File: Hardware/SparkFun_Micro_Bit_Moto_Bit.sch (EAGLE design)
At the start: 37 parts, among them J1 5.5x2.1mm Barrel, J2 CORTEX_DEBUGPTH, U1 CY8C4245LQI-483, U2 TPS62172, U3 micro:bit, U4 DRV8835

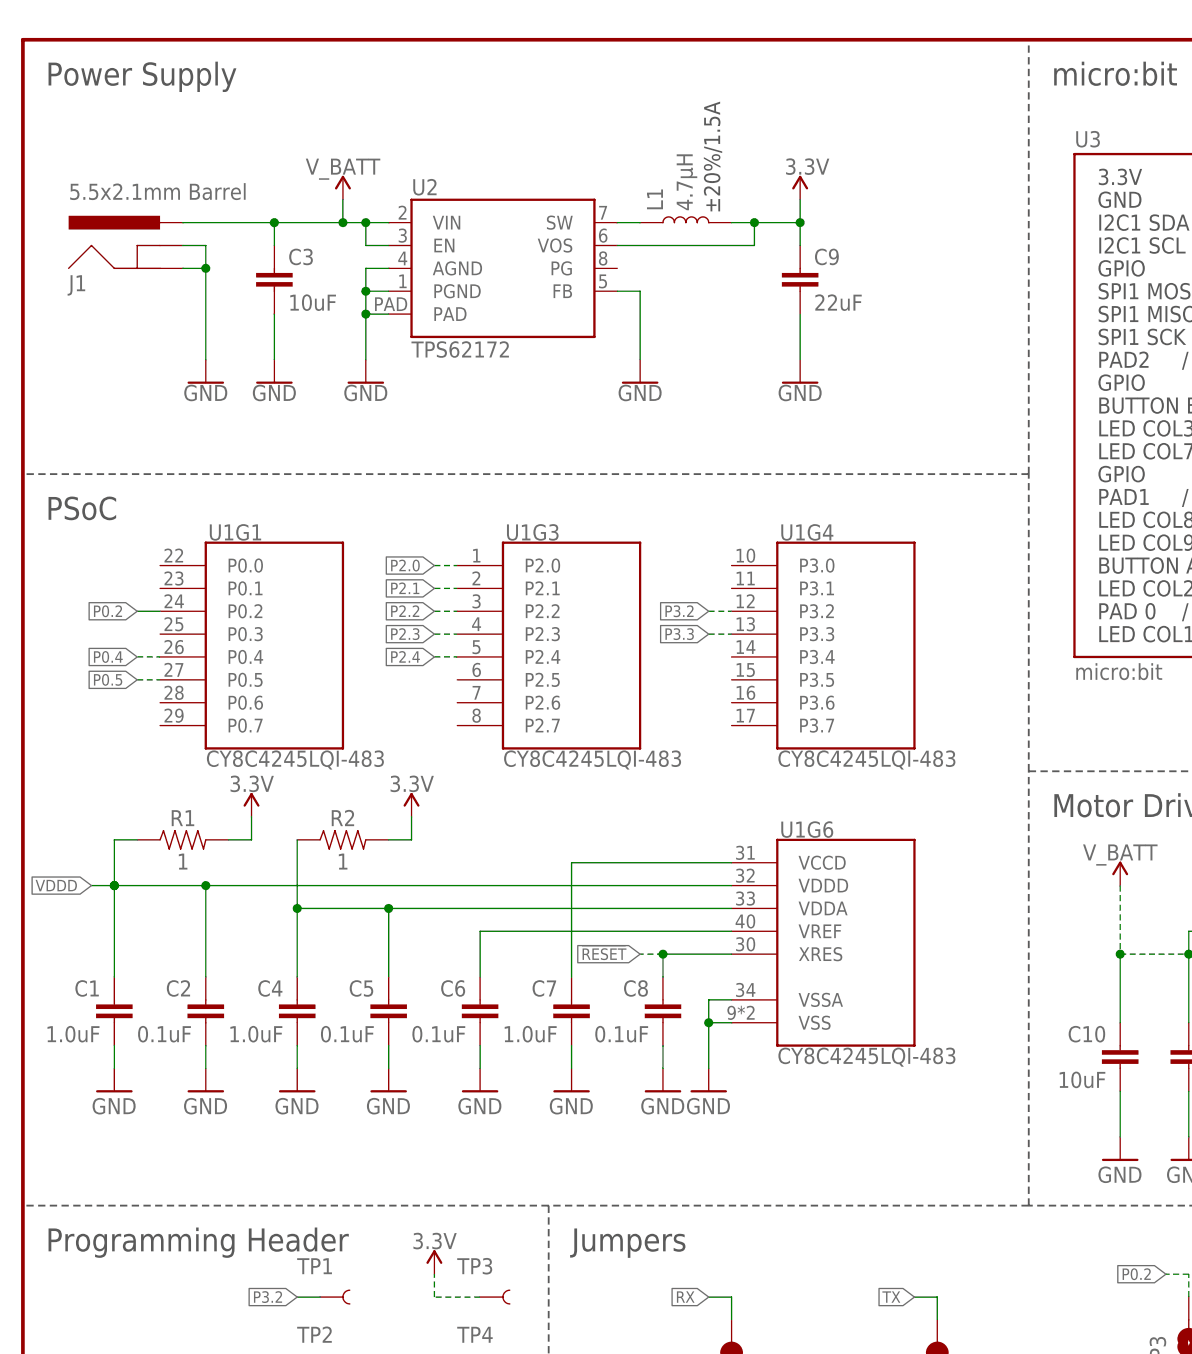
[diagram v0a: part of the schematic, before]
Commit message: Changed name from motobit to follow naming conventions
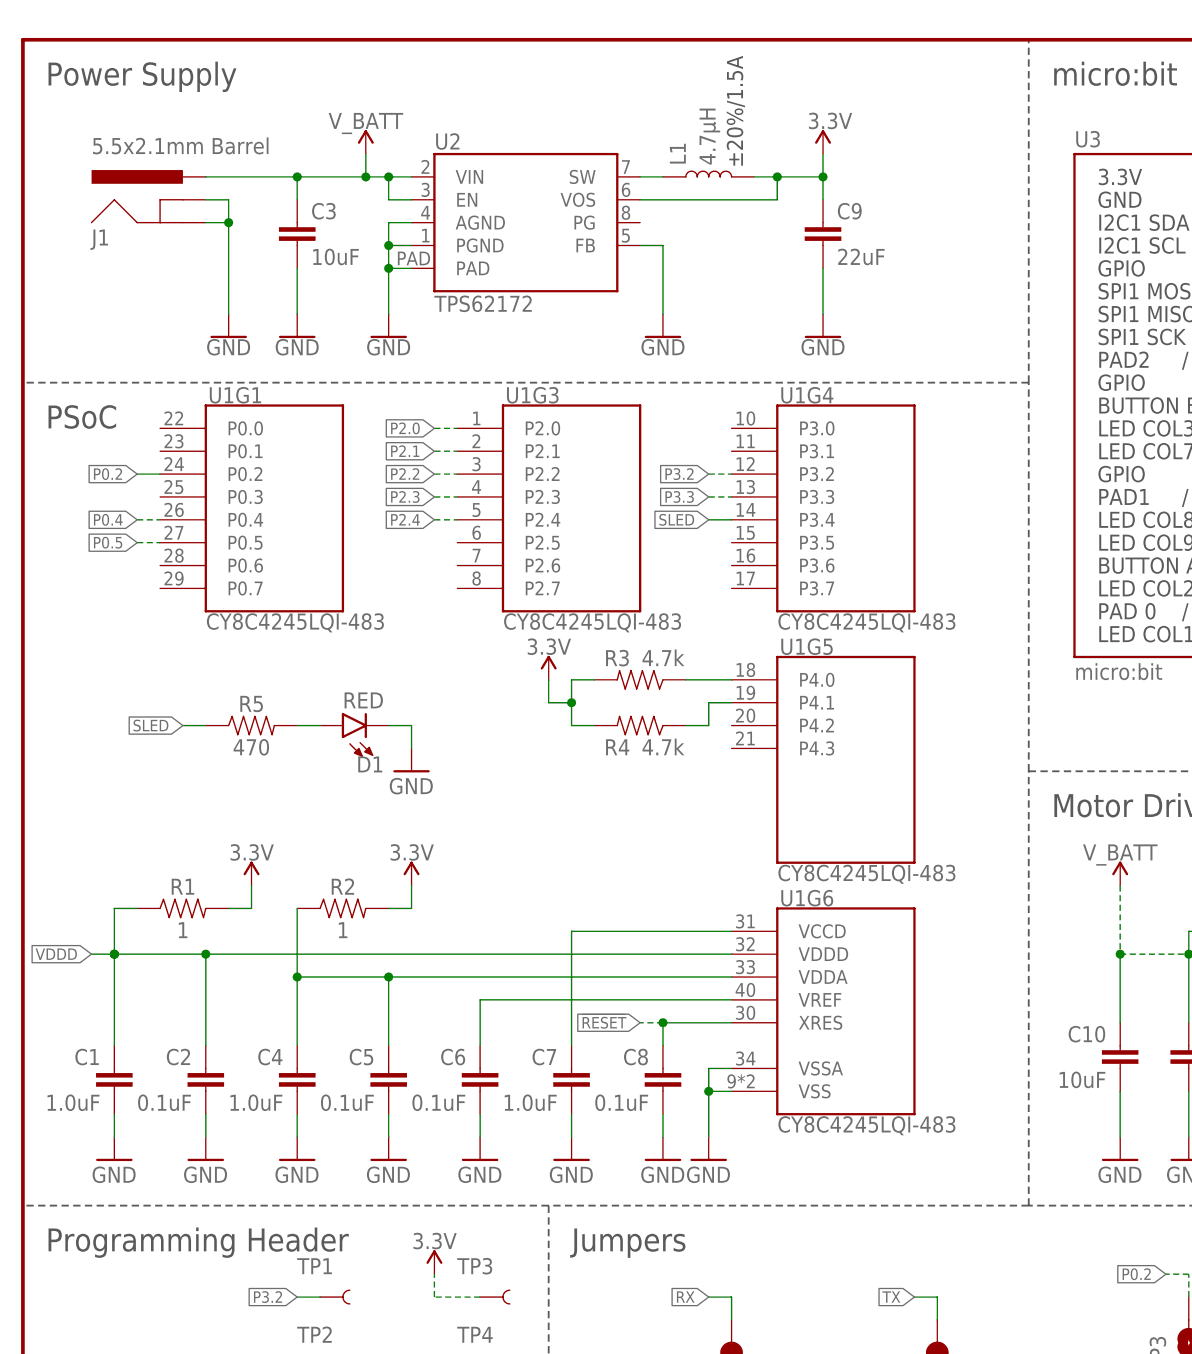
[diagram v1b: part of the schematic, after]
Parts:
- added D1: RED, SparkFun-LED:LED-RED0603
- added R3, R4: 4.7k, SparkFun-Resistors:4.7KOHM-0603-1/10W-1%
- added R5: 470, SparkFun-Resistors:470OHM-0603-1/10W-1%
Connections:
- new net N$6: R3.1, U1G5.P4.0
- new net N$7: R4.1, U1G5.P4.1
- new net N$8: D1.A, R5.2
- new net SLED: R5.1, U1G4.P3.4
- net 3.3V: now also R3.2, R4.2
- net GND: now also D1.C
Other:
- moved on the sheet: C1, C2, C3, C4, C5, C6, C7, C8, C9, J1, L1, R1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

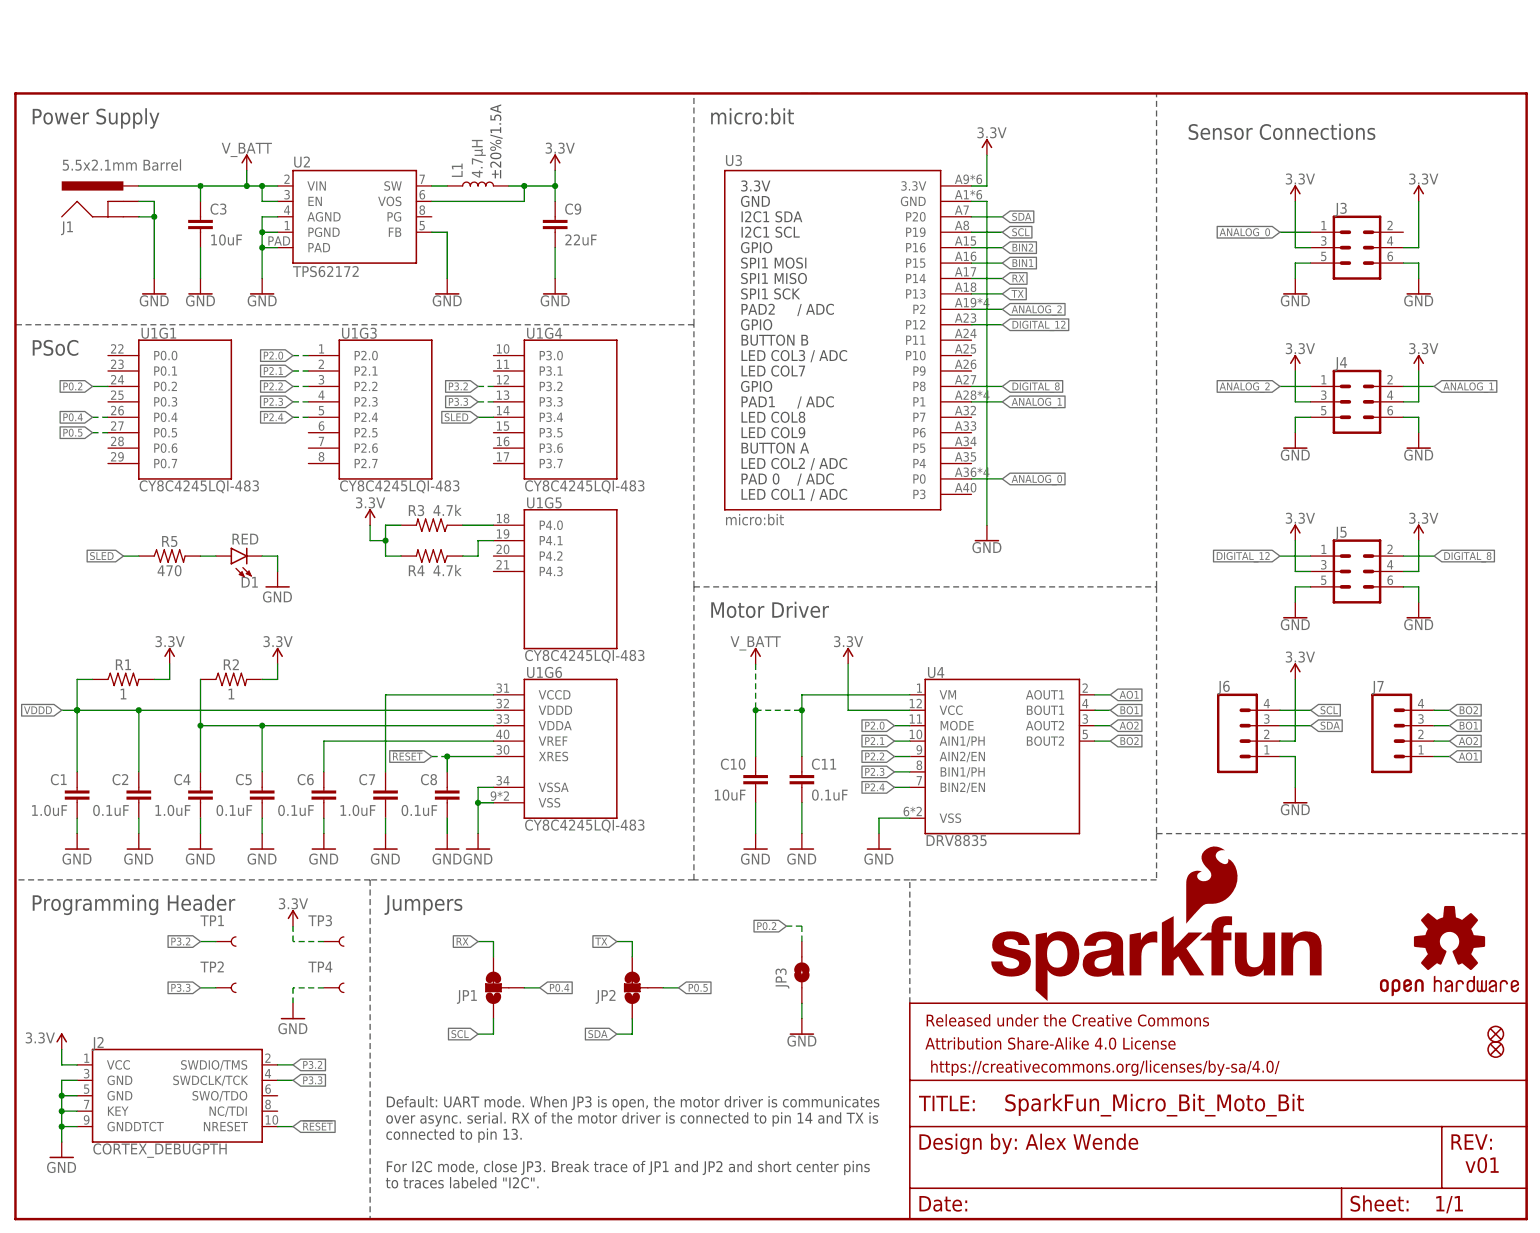
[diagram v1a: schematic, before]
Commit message: Design Review Changes
- Added staking vias to barrel connector and motor connector
- Added two servo connectors
- Moved vias that were exposed for motor driver heatsink
- Added selective solder path
- Added mounting holes
- Rounded corners to match micro:bit
- Rotated silk to match micro:bit silk orientation
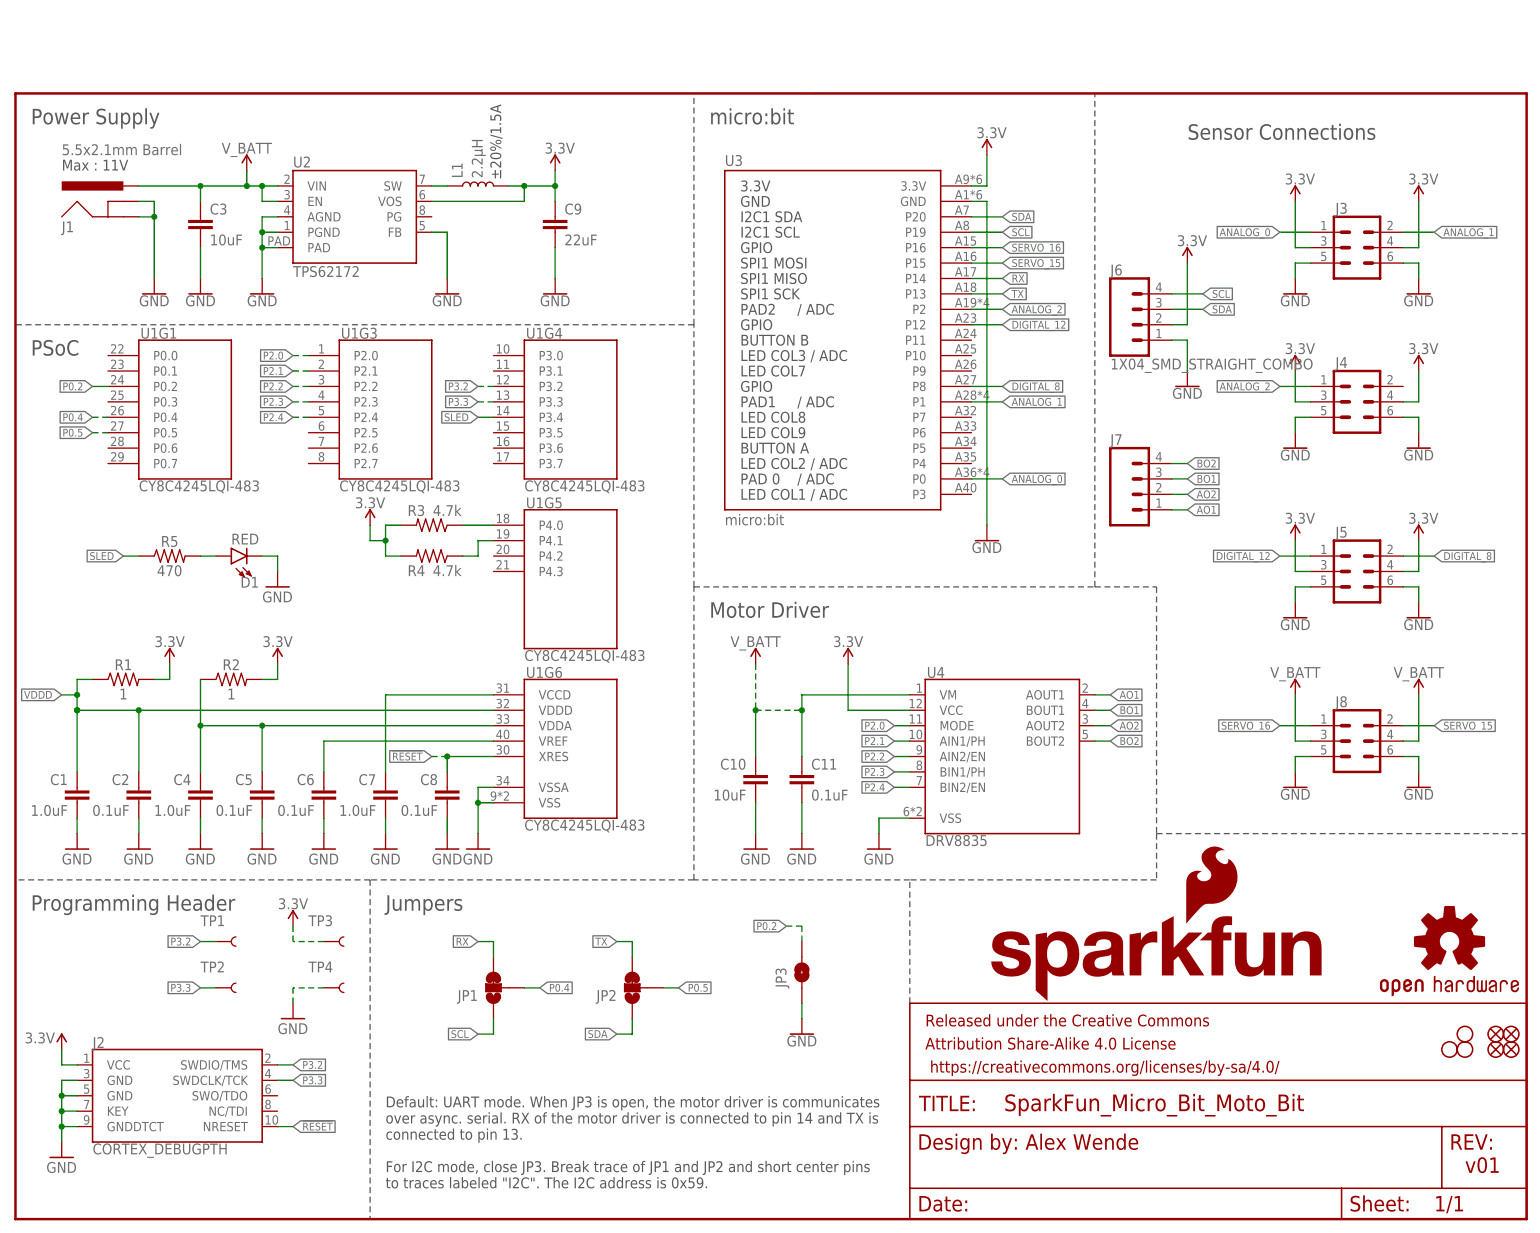
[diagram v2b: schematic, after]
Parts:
- added FD3, FD4: FIDUCIALUFIDUCIAL, SparkFun-Aesthetics:FIDUCIALUFIDUCIAL
- added H2, H3, H4: STAND-OFF, SparkFun-Hardware:STAND-OFF
- added J8: (no value), SparkFun-Connectors:CONN_03X2FEMALE_SMD
- J6: value (none) -> 1X04_SMD_STRAIGHT_COMBO
- L1: value 4.7µH -> 2.2µH
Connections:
- removed net BIN1: U3.P15
- removed net BIN2: U3.P16
- new net SERVO_15: J8.2, U3.P15
- new net SERVO_16: J8.1, U3.P16
- net ANALOG_1: now also J3.2; no longer J4.2
- net GND: now also J8.5, J8.6
- net V_BATT: now also J8.3, J8.4
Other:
- note added: "Default: UART mode. When JP3 is open, the motor driver is communicates over async. serial. RX of the motor driver is connected to pin 14 and TX is connected to pin 13. For I2C mode, close JP3. Break trace of JP1 and JP2 and short center pins to traces labeled "I2C". The I2C address is 0x59."
- note added: "Max : 11V"
- note removed: "Default: UART mode. When JP3 is open, the motor driver is communicates over async. serial. RX of the motor driver is connected to pin 14 and TX is connected to pin 13. For I2C mode, close JP3. Break trace of JP1 and JP2 and short center pins to traces labeled "I2C"."
- moved on the sheet: J6, J7

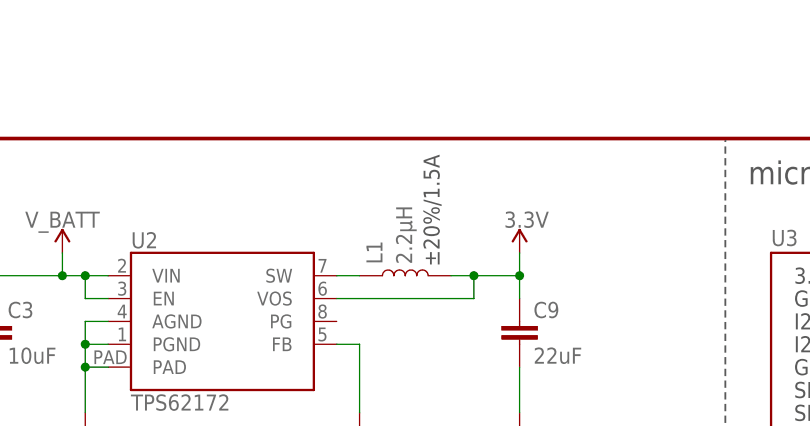
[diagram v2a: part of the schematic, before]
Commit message: QC Fixes
- Removed excess copper around PSoC center pad
- Added names and values to buck converter and inductor
- Added note about solder mask color finish
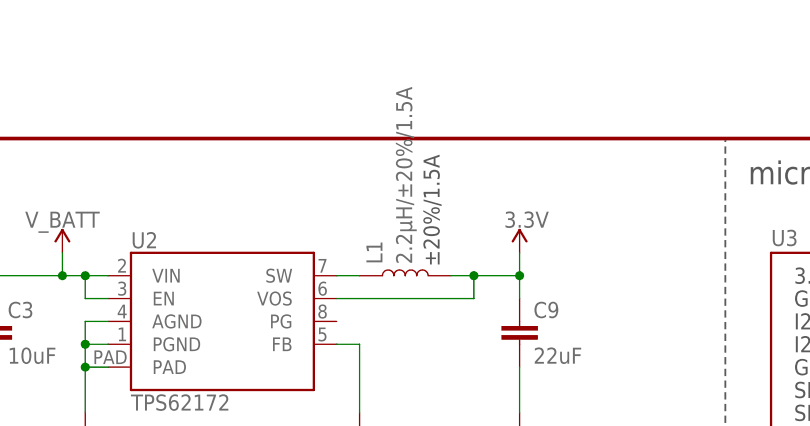
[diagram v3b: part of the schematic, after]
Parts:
- L1: value 2.2µH -> 2.2µH/±20%/1.5A
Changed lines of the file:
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@@
 <part name="U2" library="SparkFun-IC-Power" deviceset="TPS62172" device=""/>
 <part name="GND7" library="SparkFun-PowerSymbols" deviceset="GND" device=""/>
-<part name="L1" library="SparkFun-Coils" deviceset="INDUCTOR" device="-VLF4012AT-2.2UH" value="2.2µH"/>
+<part name="L1" library="SparkFun-Coils" deviceset="INDUCTOR" device="-VLF4012AT-2.2UH" value="2.2µH/±20%/1.5A"/>
 <part name="GND11" library="SparkFun-PowerSymbols" deviceset="GND" device=""/>
 <part name="C3" library="SparkFun-Capacitors" deviceset="10UF" device="-1210-50V-20%" value="10uF"/>
